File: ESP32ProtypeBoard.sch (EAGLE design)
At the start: 85 parts, among them IC2 SI4431BDY, J10 POWER_JACKPTH_LOCK, Q2 MMBT3904, Q3 MMBT3904, U2 ESP-WROOM-32

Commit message: Added place for smd logic level converter
used free space
fixed silk in bottom smd placeholder
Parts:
- added J39: (no value), SparkFun-Connectors:CONN_051.27MM
- added Q4: BSS138, bss138_10:BSS138
- added SMD3, SMD4: (no value), rcl:R-EU_R0805
- D1: value PWR ON -> PWR
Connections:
- new net N$1: J39.4, Q4.S, SMD4.2
- new net N$11: J39.3, Q4.G, SMD4.1
- new net N$12: J39.1, SMD3.1
- new net N$2: J39.2, Q4.D, SMD3.2
- net GND: now also J39.5
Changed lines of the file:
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@@
 <part name="P+3" library="supply1" library_urn="urn:adsk.eagle:library:371" deviceset="VCC" device=""/>
 <part name="R4" library="eagle-ltspice" library_urn="urn:adsk.eagle:library:217" deviceset="R" device="R1206" package3d_urn="urn:adsk.eagle:package:13301/1" value="22K"/>
-<part name="D1" library="SparkFun-LED" deviceset="LED-GREEN" device="1206" value="PWR ON"/>
+<part name="D1" library="SparkFun-LED" deviceset="LED-GREEN" device="1206" value="PWR"/>
 <part name="GND5" library="supply1" library_urn="urn:adsk.eagle:library:371" deviceset="GND" device=""/>
 <part name="+3V7" library="supply1" library_urn="urn:adsk.eagle:library:371" deviceset="+3V3" device=""/>
@@
 <part name="IO0" library="SparkFun-Connectors" library_urn="urn:adsk.eagle:library:513" deviceset="CONN_01" device="PTH_NO_SILK_KIT" package3d_urn="urn:adsk.eagle:package:38038/1"/>
 <part name="GND17" library="supply1" library_urn="urn:adsk.eagle:library:371" deviceset="GND" device=""/>
+<part name="Q4" library="bss138_10" deviceset="BSS138" device=""/>
+<part name="SMD3" library="rcl" library_urn="urn:adsk.eagle:library:334" deviceset="R-EU_" device="R0805" package3d_urn="urn:adsk.eagle:package:23553/2"/>
+<part name="SMD4" library="rcl" library_urn="urn:adsk.eagle:library:334" deviceset="R-EU_" device="R0805" package3d_urn="urn:adsk.eagle:package:23553/2"/>
+<part name="J39" library="SparkFun-Connectors" library_urn="urn:adsk.eagle:library:513" deviceset="CONN_05" device="1.27MM" package3d_urn="urn:adsk.eagle:package:38110/1"/>
+<part name="GND18" library="supply1" library_urn="urn:adsk.eagle:library:371" deviceset="GND" device=""/>
 </parts>
 <sheets>
@@
 <instance part="GND17" gate="1" x="228.6" y="71.12" smashed="yes" rot="R270">
 <attribute name="VALUE" x="226.06" y="73.66" size="1.778" layer="96" rot="R270"/>
+</instance>
+<instance part="Q4" gate="G$1" x="401.32" y="48.26" smashed="yes" rot="MR270">
+<attribute name="NAME" x="398.78" y="45.72" size="1.778" layer="95" rot="MR270"/>
+<attribute name="VALUE" x="393.7" y="50.8" size="1.778" layer="96" rot="MR180"/>
+</instance>
+<instance part="SMD3" gate="G$1" x="388.62" y="50.8" smashed="yes" rot="R270">
+<attribute name="NAME" x="390.1186" y="54.61" size="1.778" layer="95" rot="R270"/>
+<attribute name="VALUE" x="385.318" y="54.61" size="1.778" layer="96" rot="R270"/>
+</instance>
+<instance part="SMD4" gate="G$1" x="408.94" y="50.8" smashed="yes" rot="R270">
+<attribute name="NAME" x="410.4386" y="54.61" size="1.778" layer="95" rot="R270"/>
+<attribute name="VALUE" x="405.638" y="54.61" size="1.778" layer="96" rot="R270"/>
+</instance>
+<instance part="J39" gate="G$1" x="401.32" y="71.12" smashed="yes" rot="R270">
+<attribute name="VALUE" x="393.954" y="76.2" size="1.778" layer="96" font="vector" rot="R270"/>
+<attribute name="NAME" x="409.448" y="76.2" size="1.778" layer="95" font="vector" rot="R270"/>
+</instance>
+<instance part="GND18" gate="1" x="408.94" y="63.5" smashed="yes" rot="R90">
+<attribute name="VALUE" x="411.48" y="60.96" size="1.778" layer="96" rot="R90"/>
 </instance>
 </instances>
@@
 <wire x1="231.14" y1="71.12" x2="236.22" y2="71.12" width="0.1524" layer="91"/>
 </segment>
+<segment>
+<pinref part="GND18" gate="1" pin="GND"/>
+<pinref part="J39" gate="G$1" pin="5"/>
+</segment>
 </net>
 <net name="+3V3" class="0">
@@
 </segment>
 </net>
+<net name="N$1" class="0">
+<segment>
+<pinref part="Q4" gate="G$1" pin="S"/>
+<wire x1="406.4" y1="45.72" x2="408.94" y2="45.72" width="0.1524" layer="91"/>
+<pinref part="SMD4" gate="G$1" pin="2"/>
+<junction x="408.94" y="45.72"/>
+<wire x1="408.94" y1="45.72" x2="414.02" y2="45.72" width="0.1524" layer="91"/>
+<wire x1="414.02" y1="45.72" x2="414.02" y2="58.42" width="0.1524" layer="91"/>
+<pinref part="J39" gate="G$1" pin="4"/>
+<wire x1="403.86" y1="63.5" x2="403.86" y2="58.42" width="0.1524" layer="91"/>
+<wire x1="403.86" y1="58.42" x2="414.02" y2="58.42" width="0.1524" layer="91"/>
+</segment>
+</net>
+<net name="N$2" class="0">
+<segment>
+<pinref part="SMD3" gate="G$1" pin="2"/>
+<pinref part="Q4" gate="G$1" pin="D"/>
+<wire x1="388.62" y1="45.72" x2="396.24" y2="45.72" width="0.1524" layer="91"/>
+<junction x="396.24" y="45.72"/>
+<wire x1="396.24" y1="45.72" x2="396.24" y2="60.96" width="0.1524" layer="91"/>
+<pinref part="J39" gate="G$1" pin="2"/>
+<wire x1="396.24" y1="60.96" x2="398.78" y2="60.96" width="0.1524" layer="91"/>
+<wire x1="398.78" y1="60.96" x2="398.78" y2="63.5" width="0.1524" layer="91"/>
+</segment>
+</net>
+<net name="N$11" class="0">
+<segment>
+<pinref part="SMD4" gate="G$1" pin="1"/>
+<pinref part="Q4" gate="G$1" pin="G"/>
+<wire x1="403.86" y1="55.88" x2="408.94" y2="55.88" width="0.1524" layer="91"/>
+<wire x1="403.86" y1="50.8" x2="403.86" y2="55.88" width="0.1524" layer="91"/>
+<wire x1="403.86" y1="55.88" x2="401.32" y2="55.88" width="0.1524" layer="91"/>
+<junction x="403.86" y="55.88"/>
+<pinref part="J39" gate="G$1" pin="3"/>
+<wire x1="401.32" y1="55.88" x2="401.32" y2="63.5" width="0.1524" layer="91"/>
+</segment>
+</net>
+<net name="N$12" class="0">
+<segment>
+<pinref part="SMD3" gate="G$1" pin="1"/>
+<wire x1="388.62" y1="55.88" x2="388.62" y2="63.5" width="0.1524" layer="91"/>
+<pinref part="J39" gate="G$1" pin="1"/>
+<wire x1="396.24" y1="63.5" x2="388.62" y2="63.5" width="0.1524" layer="91"/>
+</segment>
+</net>

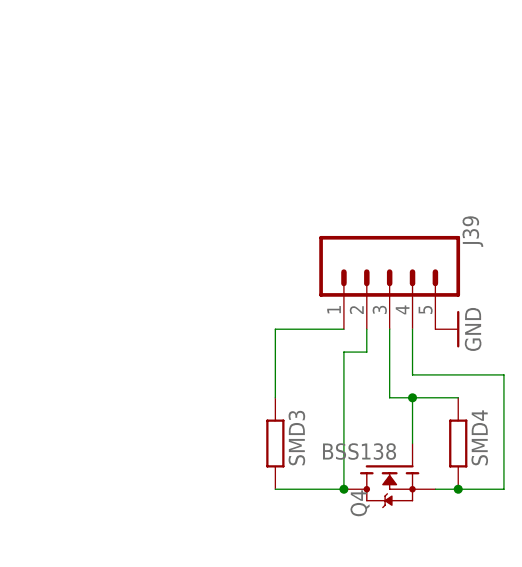
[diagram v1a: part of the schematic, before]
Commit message: removed extra gnd, added dot as orientation mark
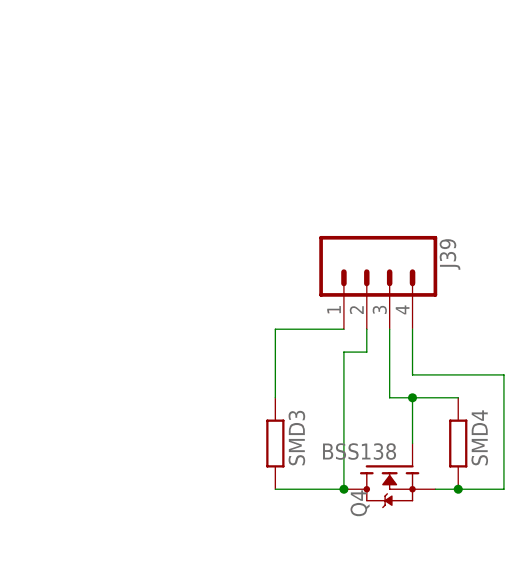
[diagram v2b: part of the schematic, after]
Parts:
- J39: device SparkFun-Connectors:CONN_051.27MM -> SparkFun-Connectors:CONN_041.27MM
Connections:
- net GND: no longer J39.5
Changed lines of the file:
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@@
 <part name="SMD3" library="rcl" library_urn="urn:adsk.eagle:library:334" deviceset="R-EU_" device="R0805" package3d_urn="urn:adsk.eagle:package:23553/2"/>
 <part name="SMD4" library="rcl" library_urn="urn:adsk.eagle:library:334" deviceset="R-EU_" device="R0805" package3d_urn="urn:adsk.eagle:package:23553/2"/>
-<part name="J39" library="SparkFun-Connectors" library_urn="urn:adsk.eagle:library:513" deviceset="CONN_05" device="1.27MM" package3d_urn="urn:adsk.eagle:package:38110/1"/>
-<part name="GND18" library="supply1" library_urn="urn:adsk.eagle:library:371" deviceset="GND" device=""/>
+<part name="J39" library="SparkFun-Connectors" library_urn="urn:adsk.eagle:library:513" deviceset="CONN_04" device="1.27MM" package3d_urn="urn:adsk.eagle:package:38086/1"/>
 </parts>
 <sheets>
@@
 <attribute name="VALUE" x="405.638" y="54.61" size="1.778" layer="96" rot="R270"/>
 </instance>
-<instance part="J39" gate="G$1" x="401.32" y="71.12" smashed="yes" rot="R270">
-<attribute name="VALUE" x="393.954" y="76.2" size="1.778" layer="96" font="vector" rot="R270"/>
-<attribute name="NAME" x="409.448" y="76.2" size="1.778" layer="95" font="vector" rot="R270"/>
-</instance>
-<instance part="GND18" gate="1" x="408.94" y="63.5" smashed="yes" rot="R90">
-<attribute name="VALUE" x="411.48" y="60.96" size="1.778" layer="96" rot="R90"/>
+<instance part="J39" gate="G$1" x="398.78" y="68.58" smashed="yes" rot="R270">
+<attribute name="VALUE" x="391.414" y="73.66" size="1.778" layer="96" font="vector" rot="R270"/>
+<attribute name="NAME" x="406.908" y="73.66" size="1.778" layer="95" font="vector" rot="R270"/>
 </instance>
 </instances>
@@
 <wire x1="231.14" y1="71.12" x2="236.22" y2="71.12" width="0.1524" layer="91"/>
 </segment>
-<segment>
-<pinref part="GND18" gate="1" pin="GND"/>
-<pinref part="J39" gate="G$1" pin="5"/>
-</segment>
 </net>

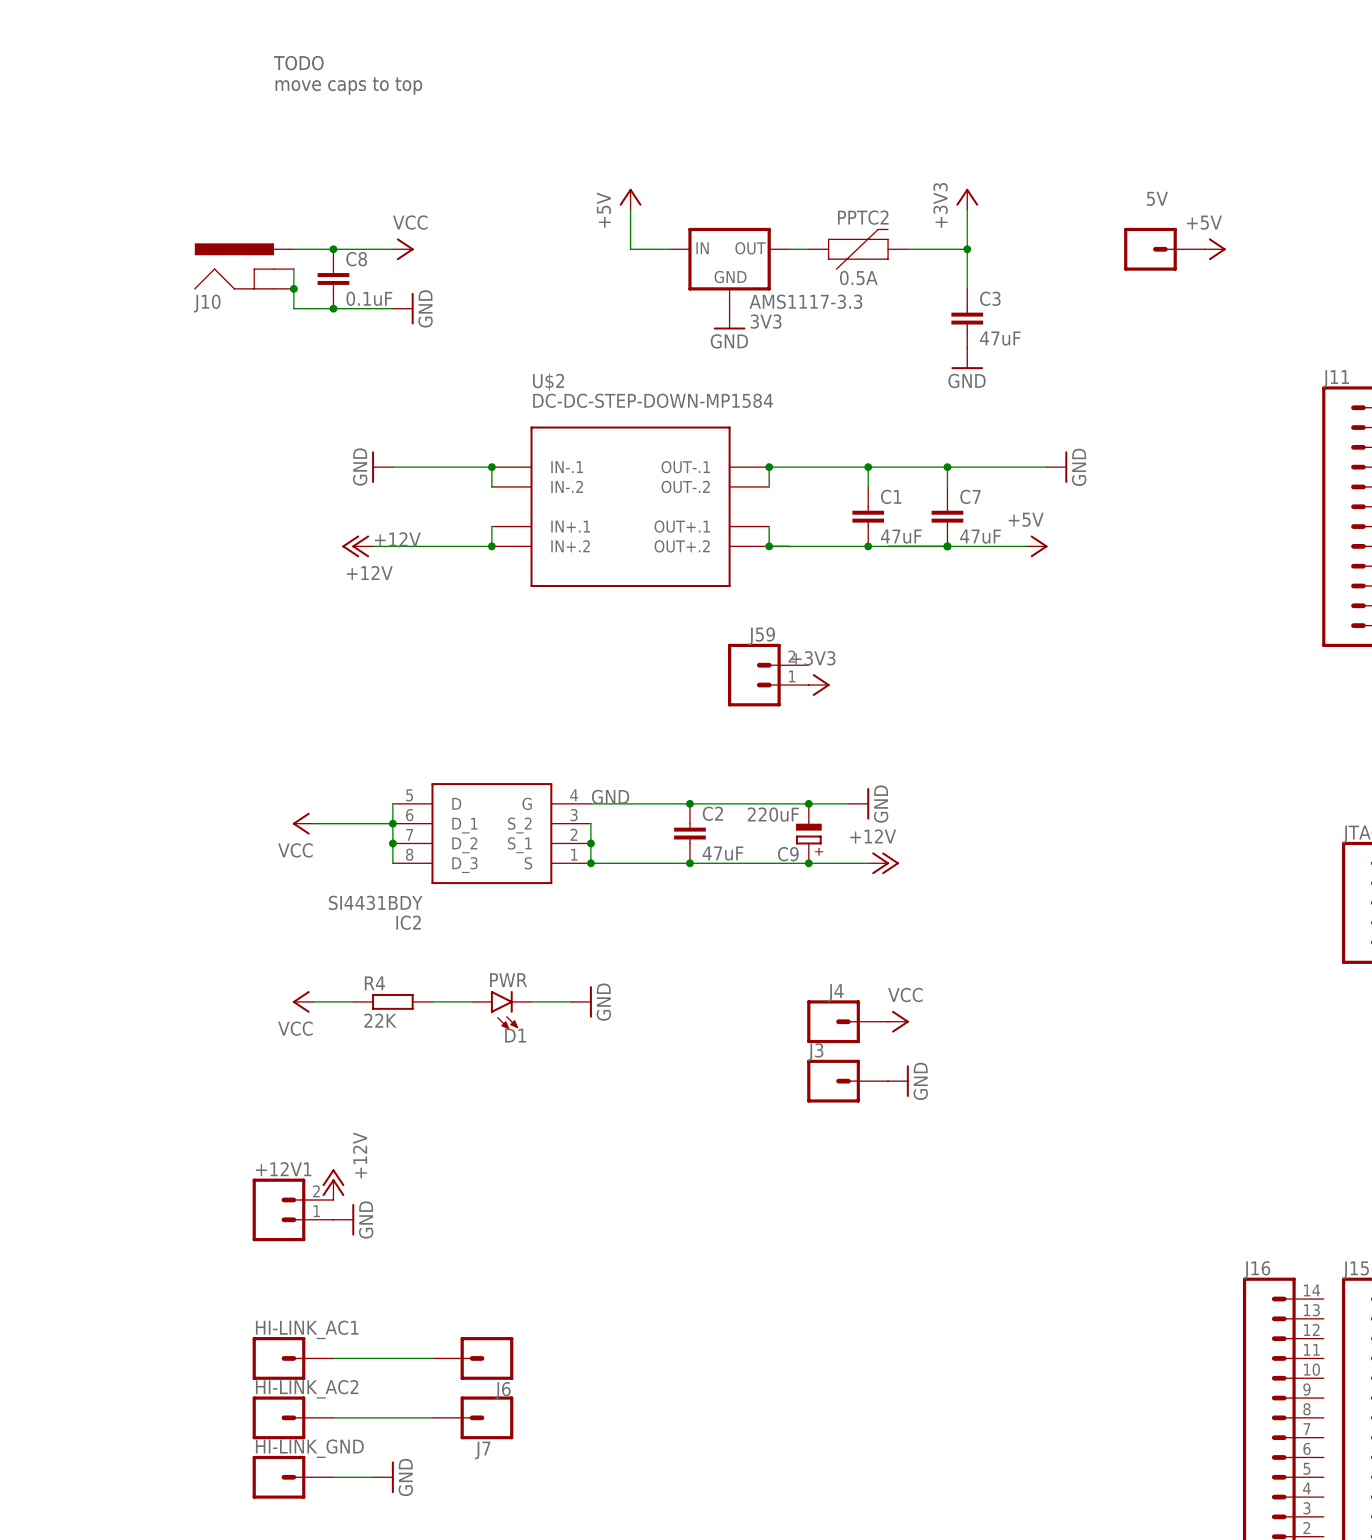
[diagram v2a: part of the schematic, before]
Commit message: Removed input 220uF cap (should work without)
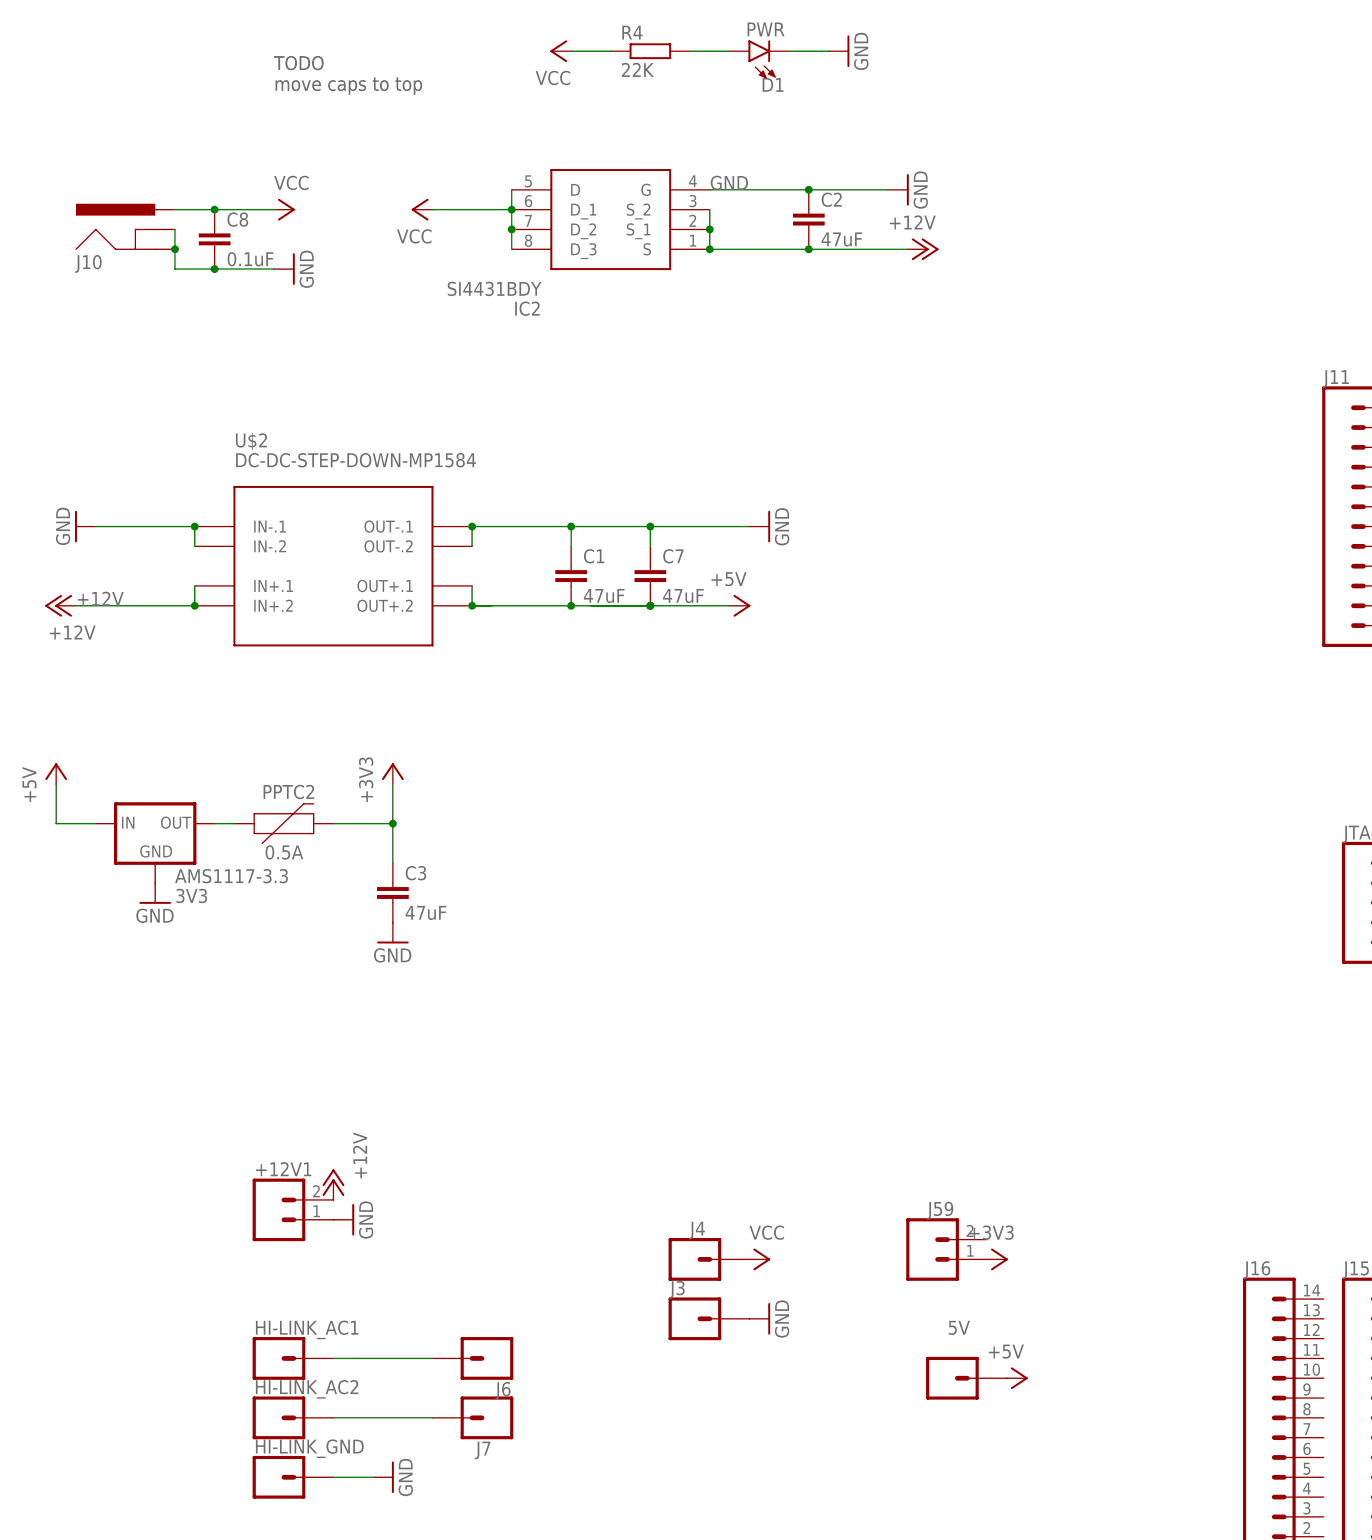
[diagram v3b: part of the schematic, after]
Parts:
- removed C9: 220uF, rcl:CPOL-EUE2.5-6
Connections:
- net +12V: no longer C9.+
- net GND: no longer C9.-
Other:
- moved on the sheet: 5V, AMS1117-3.3, C1, C2, C3, C7, C8, D1, IC2, J10, J3, J4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
